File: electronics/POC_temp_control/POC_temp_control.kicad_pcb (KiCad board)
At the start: 2 copper layers, 109.2 x 78.7 mm, 206 parts, among them J1 Conn_01x02, J2 Conn_01x07, J3 Conn_01x05, J4 Conn_01x06, J5 Conn_01x04, J6 Conn_01x06, Q1 PXT8050, Q10 BC847A, Q11 BC858B, Q12 BC847A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

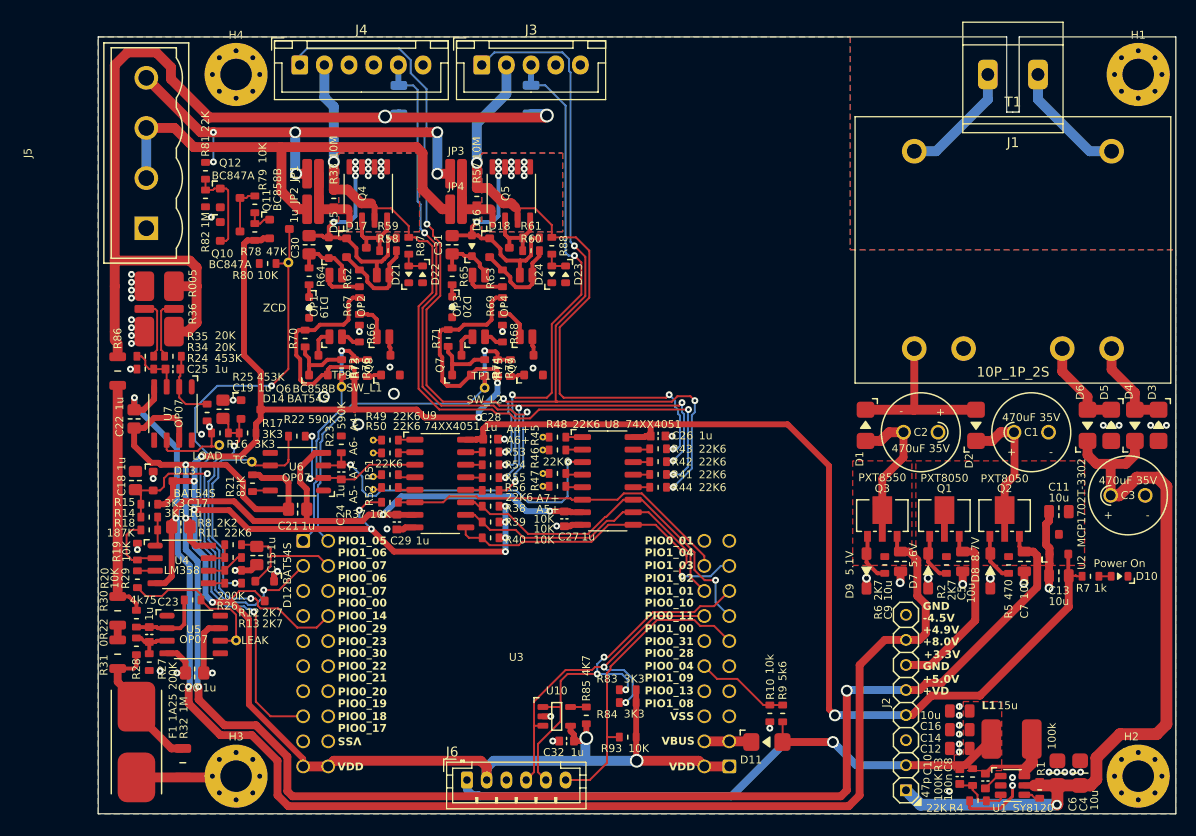
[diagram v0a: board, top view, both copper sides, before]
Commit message: updated silk placement
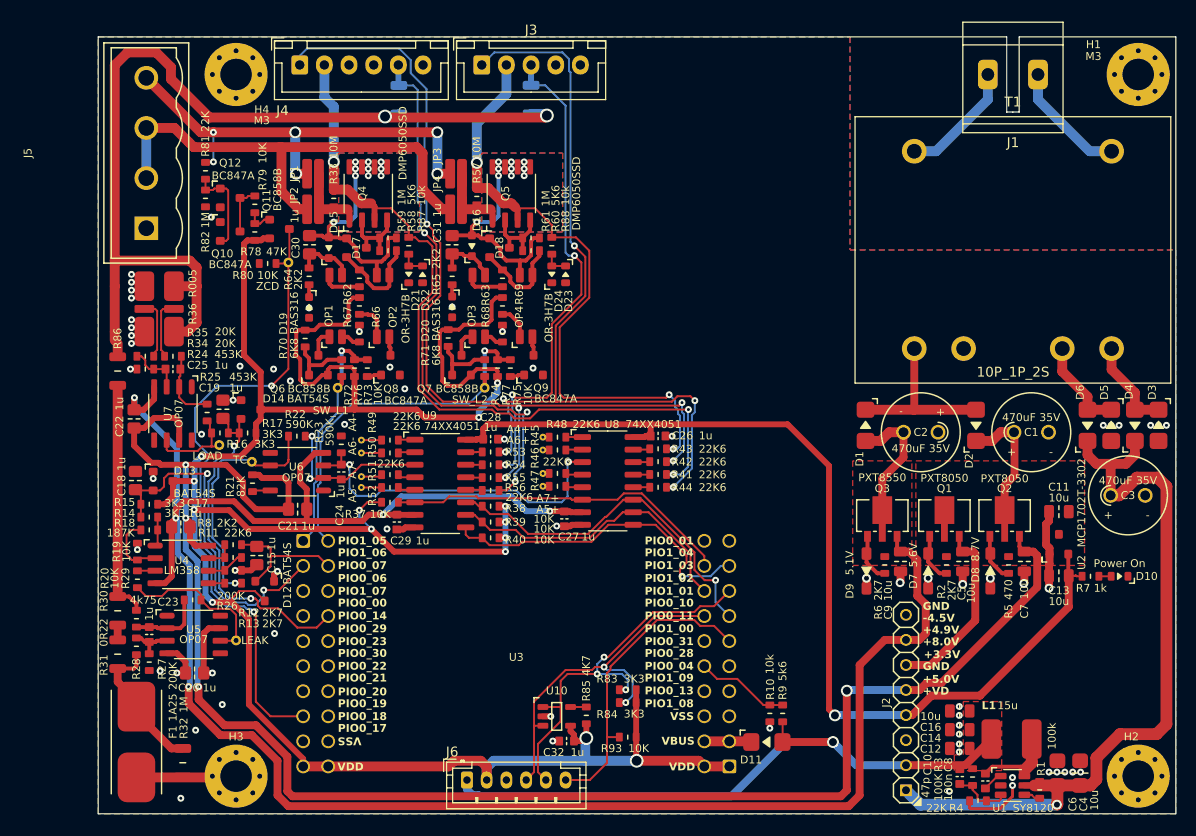
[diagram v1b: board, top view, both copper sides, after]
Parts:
- OP1, OP2, OP3, OP4: value ~ -> OR-3H7B
- Q4, Q5: value Q_PMOS_DUAL -> DMP6050SSD
- moved TP8 1.22 mm to (50.8, 69.8)
- moved TP5 1.20 mm to (50.8, 65.0)
- moved TP6 1.20 mm to (50.8, 66.3)
- moved TP7 1.20 mm to (50.8, 68.7)
- moved TP9 0.41 mm to (48.4, 59.7)
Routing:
- net Net-(R50-Pad1): track 0.85 -> 2.05 mm
- net Net-(R49-Pad1): track 0.85 -> 2.05 mm
- net Net-(R51-Pad1): track 0.93 -> 2.13 mm
- net Net-(R52-Pad1): track 0.93 -> 2.05 mm
- net /TC+DIFF: track 34.0 -> 34.6 mm
- net /LOAD_DIFF: vias 1 -> 0
- net /GND: vias 60 -> 66

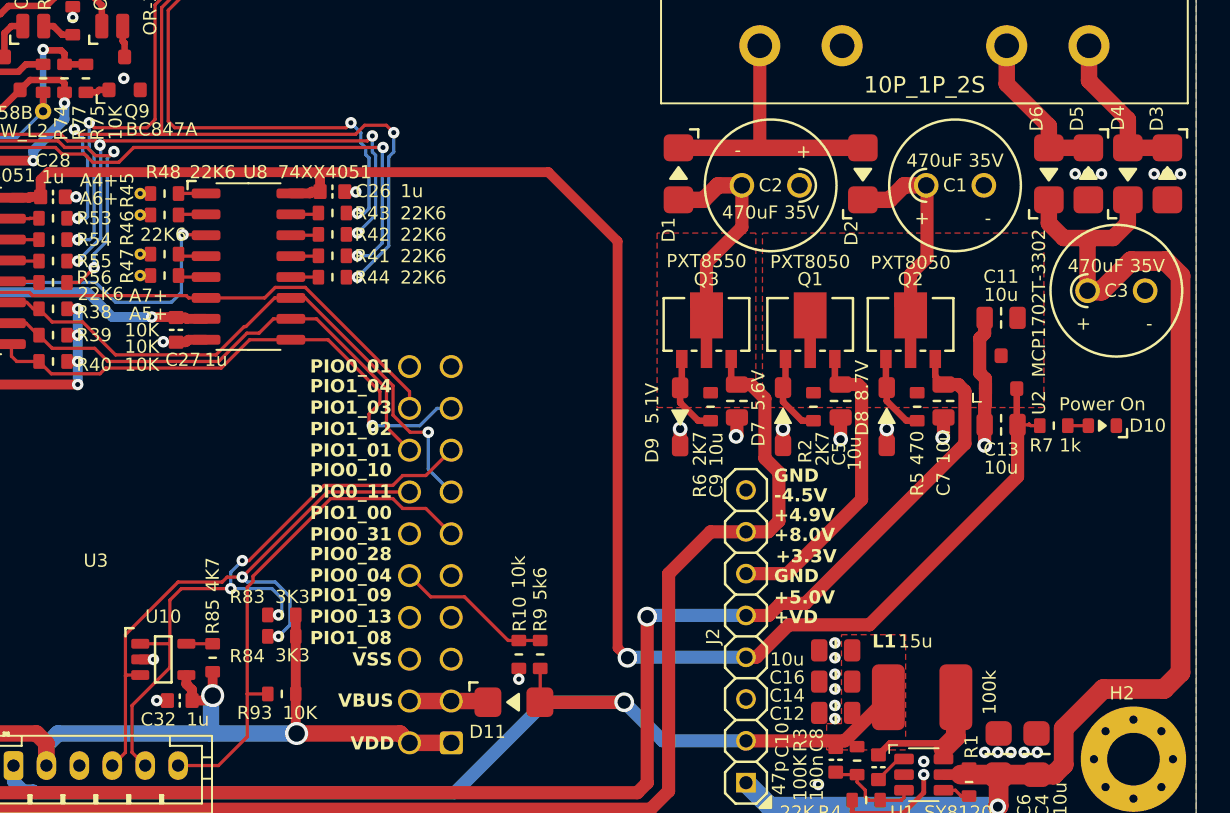
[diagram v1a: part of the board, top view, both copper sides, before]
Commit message: added values to all components
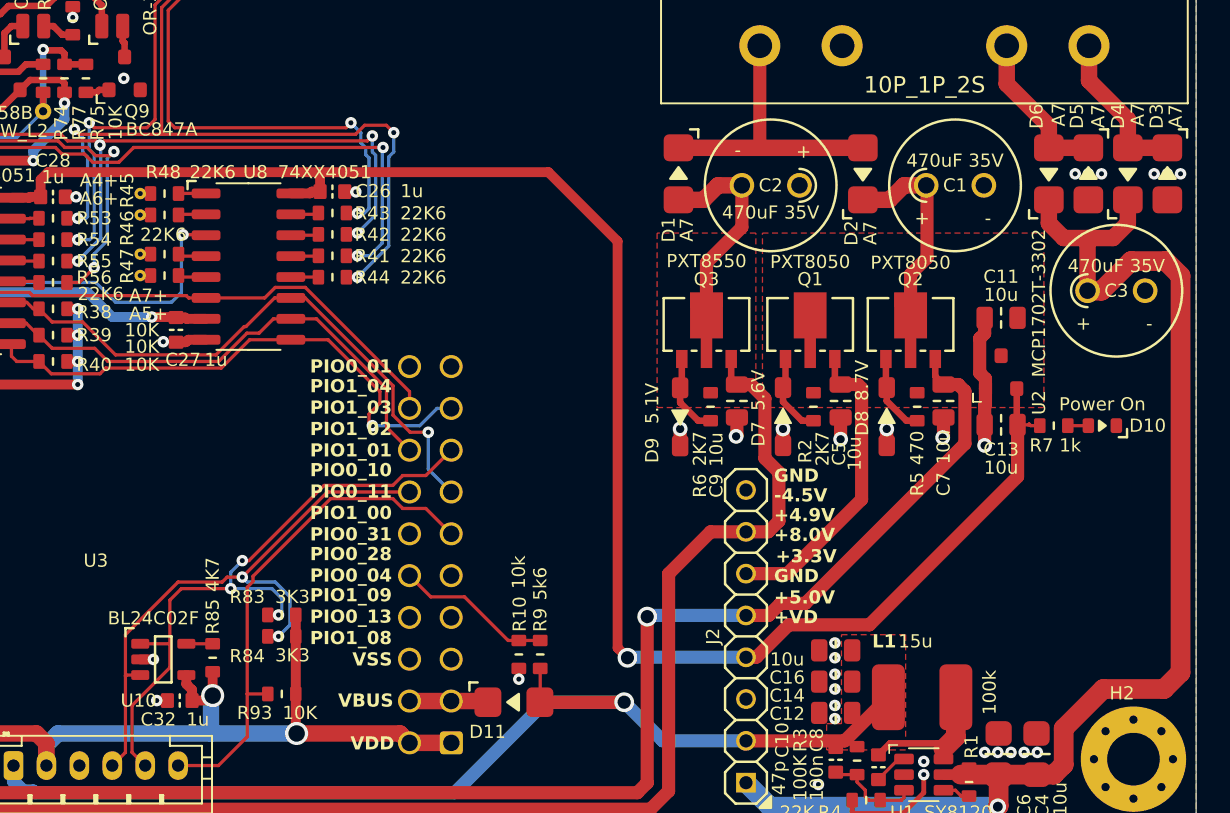
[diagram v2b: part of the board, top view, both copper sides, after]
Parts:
- D1, D11, D2, D3, D4, D5, D6: value D -> A7
- N2: value 20240927 -> 20240504
- U10: value ~ -> BL24C02F
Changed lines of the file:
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@@
 			)
 		)
-		(property "Value" "D"
-			(at -3.5 0.45 90)
-			(layer "F.Fab")
+		(property "Value" "A7"
+			(at -3.6 0.45 90)
+			(layer "F.SilkS")
 			(effects
 				(font
@@
 		(tags "SOD-123F handsoldering")
 		(property "Reference" "D5"
-			(at -3.35 0.7 90)
+			(at -3.5 0.7 90)
 			(layer "F.SilkS")
 			(effects
@@
 			)
 		)
-		(property "Value" "D"
-			(at 0 1.8 90)
-			(layer "F.Fab")
+		(property "Value" "A7"
+			(at -3.5 -0.6 90)
+			(layer "F.SilkS")
 			(effects
 				(font
@@
 			)
 		)
-		(property "Value" "D"
-			(at 3.15 -0.6 90)
-			(layer "F.Fab")
+		(property "Value" "A7"
+			(at 3.4 -0.5 90)
+			(layer "F.SilkS")
 			(effects
 				(font
@@
 		(tags "SOD-123F handsoldering")
 		(property "Reference" "D4"
-			(at 3.4 -0.6 90)
+			(at 3.5 -0.6 90)
 			(layer "F.SilkS")
 			(effects
@@
 			)
 		)
-		(property "Value" "D"
-			(at 0 1.8 90)
-			(layer "F.Fab")
+		(property "Value" "A7"
+			(at 3.6 0.6 90)
+			(layer "F.SilkS")
 			(effects
 				(font
@@
 		(tags "SOD-123F handsoldering")
 		(property "Reference" "D3"
-			(at -3.35 0.65 90)
+			(at -3.5 0.65 90)
 			(layer "F.SilkS")
 			(effects
@@
 			)
 		)
-		(property "Value" "D"
-			(at 0 1.8 90)
-			(layer "F.Fab")
+		(property "Value" "A7"
+			(at -3.5 -0.5 90)
+			(layer "F.SilkS")
 			(effects
 				(font
@@
 		(tags "Microchip SOT23 OT")
 		(property "Reference" "U10"
-			(at 0 -2.6 0)
+			(at -1.5 2.5 0)
 			(layer "F.SilkS")
 			(effects
@@
 			)
 		)
-		(property "Value" "~"
-			(at 0 2.4 0)
-			(layer "F.Fab")
+		(property "Value" "BL24C02F"
+			(at -0.6 -2.5 0)
+			(layer "F.SilkS")
 			(effects
 				(font
@@
 			)
 		)
-		(property "Value" "D"
+		(property "Value" "A7"
 			(at 0 1.8 0)
 			(layer "F.Fab")
@@
 		(tags "SOD-123F handsoldering")
 		(property "Reference" "D6"
-			(at 3.35 -0.75 90)
+			(at 3.5 -0.75 90)
 			(layer "F.SilkS")
 			(effects
@@
 			)
 		)
-		(property "Value" "D"
-			(at 0 1.8 90)
-			(layer "F.Fab")
+		(property "Value" "A7"
+			(at 3.6 0.6 90)
+			(layer "F.SilkS")
 			(effects
 				(font
@@
 		(sheetname "Root")
 		(sheetfile "POC_temp_control.kicad_sch")
-		(attr exclude_from_pos_files exclude_from_bom allow_missing_courtyard)
+		(attr exclude_from_pos_files allow_missing_courtyard)
 		(fp_poly
 			(pts
@@
 			)
 		)
-		(property "Value" "20240927"
+		(property "Value" "20240504"
 			(at 0 0 0)
 			(unlocked yes)

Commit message: preparing for production
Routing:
- net /GND: vias 66 -> 80
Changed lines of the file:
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@@
 		(tags "resistor 0603")
 		(property "Reference" "R15"
-			(at -2.5 -0.2 0)
+			(at -3.5 -2.1 0)
 			(layer "F.SilkS")
 			(effects
@@
 		)
 		(property "Value" "3K3"
-			(at 2.6 0.9 0)
+			(at -3.5 -1.1 0)
 			(layer "F.SilkS")
 			(effects
@@
 		(tags "resistor 0603")
 		(property "Reference" "R14"
-			(at 2.5 0.4 0)
+			(at 2.5 1.4 0)
 			(layer "F.SilkS")
 			(effects
@@
 		)
 		(property "Value" "3K3"
-			(at -2.6 1.4 0)
+			(at 2.5 0.4 0)
 			(layer "F.SilkS")
 			(effects
@@
 		(tags "capacitor 0805 0603 mixed")
 		(property "Reference" "C17"
-			(at 1.7 -2.4 0)
+			(at -0.7 -1.4 0)
 			(layer "F.SilkS")
 			(effects
@@
 		(tags "capacitor 0805 0603 mixed")
 		(property "Reference" "C21"
-			(at 0.94 -1.7 0)
+			(at 1.24 -1.7 0)
 			(layer "F.SilkS")
 			(effects
@@
 		)
 		(property "Value" "1u"
-			(at -1.06 -1.7 0)
+			(at -1.26 -1.7 0)
 			(layer "F.SilkS")
 			(effects
@@
 		)
 		(fp_text user "VSS"
-			(at 16.9 -8.5 180)
+			(at 16.9 -8.5 0)
 			(unlocked yes)
 			(layer "B.SilkS")
@@
 		)
 		(fp_text user "VSS"
-			(at 16.9 -8.5 180)
+			(at 16.9 -8.5 0)
 			(unlocked yes)
 			(layer "F.SilkS")
@@
 		(tags "capacitor 0805 0603 mixed")
 		(property "Reference" "C18"
-			(at -0.5 -1.4 90)
+			(at 2.8 -0.5 90)
 			(layer "F.SilkS")
 			(effects
@@
 		)
 		(property "Value" "1u"
-			(at 1.7 -1.4 90)
+			(at 2.5 0.5 90)
 			(layer "F.SilkS")
 			(effects
@@
 	)
 	(via
+		(at 102.4 99)
+		(size 0.7)
+		(drill 0.3)
+		(layers "F.Cu" "B.Cu")
+		(free yes)
+		(net 2)
+	)
+	(via
+		(at 58.8 88.1)
+		(size 0.7)
+		(drill 0.3)
+		(layers "F.Cu" "B.Cu")
+		(free yes)
+		(net 2)
+	)
+	(via
 		(at 42.3 78.3)
 		(size 0.7)
@@
 	)
 	(via
+		(at 98.6 97.2)
+		(size 0.7)
+		(drill 0.3)
+		(layers "F.Cu" "B.Cu")
+		(free yes)
+		(net 2)
+	)
+	(via
+		(at 72.6 81.7)
+		(size 0.7)
+		(drill 0.3)
+		(layers "F.Cu" "B.Cu")
+		(free yes)
+		(net 2)
+	)
+	(via
+		(at 67.5 96.3)
+		(size 0.7)
+		(drill 0.3)
+		(layers "F.Cu" "B.Cu")
+		(free yes)
+		(net 2)
+	)
+	(via
+		(at 74.8 96.3)
+		(size 0.7)
+		(drill 0.3)
+		(layers "F.Cu" "B.Cu")
+		(free yes)
+		(net 2)
+	)
+	(via
 		(at 36.7 91.8)
 		(size 0.7)
@@
 	)
 	(via
+		(at 75.9 98.7)
+		(size 0.7)
+		(drill 0.3)
+		(layers "F.Cu" "B.Cu")
+		(free yes)
+		(net 2)
+	)
+	(via
 		(at 123.7 98.65)
 		(size 0.7)
@@
 	)
 	(via
+		(at 98.9 94.2)
+		(size 0.7)
+		(drill 0.3)
+		(layers "F.Cu" "B.Cu")
+		(free yes)
+		(net 2)
+	)
+	(via
+		(at 51.4 75)
+		(size 0.7)
+		(drill 0.3)
+		(layers "F.Cu" "B.Cu")
+		(free yes)
+		(net 2)
+	)
+	(via
 		(at 117.95 79.525)
 		(size 0.9)
@@
 	)
 	(via
+		(at 100.1 89)
+		(size 0.7)
+		(drill 0.3)
+		(layers "F.Cu" "B.Cu")
+		(free yes)
+		(net 2)
+	)
+	(via
 		(at 27.5 49.8)
 		(size 0.7)
@@
 	)
 	(via
-		(at 29.7 68.9)
+		(at 28.9 68.2)
 		(size 0.7)
 		(drill 0.3)
@@
 	)
 	(via
+		(at 80.3 74.4)
+		(size 0.7)
+		(drill 0.3)
+		(layers "F.Cu" "B.Cu")
+		(free yes)
+		(net 2)
+	)
+	(via
+		(at 80.8 70.8)
+		(size 0.7)
+		(drill 0.3)
+		(layers "F.Cu" "B.Cu")
+		(free yes)
+		(net 2)
+	)
+	(via
 		(at 116.8 99.2)
 		(size 0.7)
@@
 	)
 	(via
+		(at 76.5 96.3)
+		(size 0.7)
+		(drill 0.3)
+		(layers "F.Cu" "B.Cu")
+		(free yes)
+		(net 2)
+	)
+	(via
 		(at 108.25 79)
 		(size 0.9)
@@
 	)
 	(via
+		(at 66.4 76.5)
+		(size 0.7)
+		(drill 0.3)
+		(layers "F.Cu" "B.Cu")
+		(free yes)
+		(net 2)
+	)
+	(via
 		(at 105.4 79.45)
 		(size 0.9)
@@
 	)
 	(segment
+		(start 33 67.5)
+		(end 31.433908 67.5)
+		(width 0.6)
+		(layer "F.Cu")
+		(net 16)
+	)
+	(segment
 		(start 118 76.3)
 		(end 118.9 76.3)
@@
 	)
 	(segment
+		(start 30.533908 66.6)
+		(end 28.5 66.6)
+		(width 0.6)
+		(layer "F.Cu")
+		(net 16)
+	)
+	(segment
 		(start 118 76.3)
 		(end 117.5 75.8)
@@
 	)
 	(segment
-		(start 29.5 67.3)
-		(end 27.765 65.565)
+		(start 34.825 84.575)
+		(end 35.335 84.065)
 		(width 0.6)
 		(layer "F.Cu")
@@
 	)
 	(segment
-		(start 34.825 84.575)
-		(end 35.335 84.065)
+		(start 43.415 69.315)
+		(end 42.935 68.835)
 		(width 0.6)
 		(layer "F.Cu")
@@
 	)
 	(segment
-		(start 43.415 69.315)
-		(end 42.935 68.835)
+		(start 28.5 66.6)
+		(end 27.765 65.865)
 		(width 0.6)
 		(layer "F.Cu")
@@
 	)
 	(segment
-		(start 30.267816 67.3)
-		(end 29.5 67.3)
-		(width 0.6)
-		(layer "F.Cu")
-		(net 16)
-	)
-	(segment
 		(start 99.4 101.1)
 		(end 43.814214 101.1)
@@
 	)
 	(segment
-		(start 30.467816 67.5)
-		(end 30.267816 67.3)
-		(width 0.6)
-		(layer "F.Cu")
-		(net 16)
-	)
-	(segment
 		(start 31.875 62.75)
 		(end 29.8 62.75)
@@
 	)
 	(segment
+		(start 31.433908 67.5)
+		(end 30.533908 66.6)
+		(width 0.6)
+		(layer "F.Cu")
+		(net 16)
+	)
+	(segment
 		(start 40.415 68.515)
 		(end 40.735 68.835)
@@
 	)
 	(segment
-		(start 119.3 76.7)
-		(end 119.3 79.9)
-		(width 0.8)
+		(start 27.765 65.865)
+		(end 27.765 63.775)
+		(width 0.6)
 		(layer "F.Cu")
 		(net 16)
 	)
 	(segment
-		(start 33 67.5)
-		(end 30.467816 67.5)
-		(width 0.6)
+		(start 119.3 76.7)
+		(end 119.3 79.9)
+		(width 0.8)
 		(layer "F.Cu")
 		(net 16)
@@
 	)
 	(segment
-		(start 27.765 65.565)
-		(end 27.765 63.775)
-		(width 0.6)
-		(layer "F.Cu")
-		(net 16)
-	)
-	(segment
 		(start 43.300001 97.085787)
 		(end 40.114214 93.9)
@@
 	)
 	(segment
-		(start 73.5 95.3)
-		(end 73.6 95.2)
-		(width 1)
-		(layer "B.Cu")
-		(net 26)
-	)
-	(segment
 		(start 33.9 69.2)
 		(end 33.9 72)
@@
 	)
 	(segment
+		(start 73.6 97.4)
+		(end 73.6 95.2)
+		(width 1)
+		(layer "B.Cu")
+		(net 26)
+	)
+	(segment
 		(start 50.6 72.1)
 		(end 50.6 72.8)
@@
 	)
 	(segment
-		(start 73.5 97.5)
-		(end 73.5 95.3)
-		(width 1)
-		(layer "B.Cu")
-		(net 26)
-	)
-	(segment
 		(start 35 76.9)
 		(end 33.9 75.8)
@@
 		(width 1)
 		(layer "B.Cu")
+		(net 26)
+	)
+	(segment
+		(start 73.5 97.5)
+		(end 73.6 97.4)
+		(width 1)
+		(layer "B.Cu")
